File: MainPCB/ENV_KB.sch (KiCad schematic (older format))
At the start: 196 parts

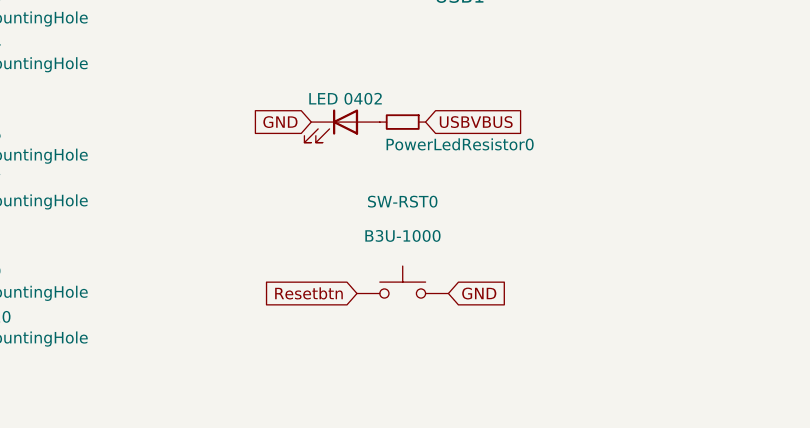
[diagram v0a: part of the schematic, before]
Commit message: Swapped Reset button for cheaper Alps SKRK
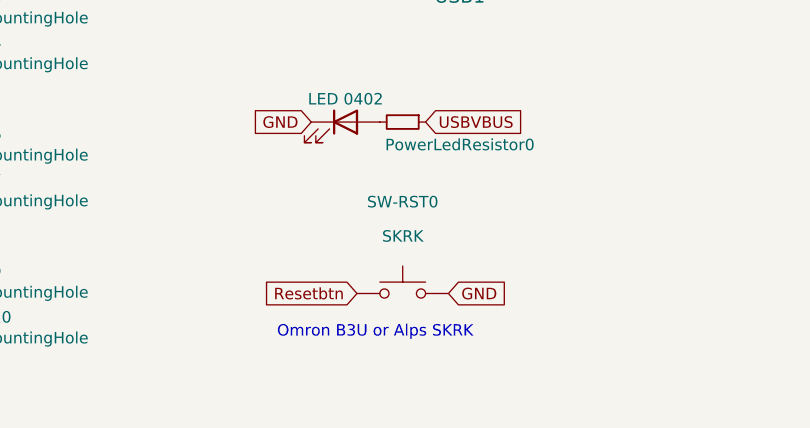
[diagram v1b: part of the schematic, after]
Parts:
- SW-RST0: value B3U-1000 -> SKRK; footprint Button_Switch_SMD:SW_SPST_B3U-1000P -> Button_Switch_SMD:SW_Push_SPST_NO_Alps_SKRK
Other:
- note added: "Omron B3U or Alps SKRK"
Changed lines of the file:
@@
 P 8550 10700
 F 0 "SW-RST0" H 8550 11100 50  0000 C CNN
-F 1 "B3U-1000" H 8550 10950 50  0000 C CNN
-F 2 "Button_Switch_SMD:SW_SPST_B3U-1000P" H 8550 10700 50  0001 L BNN
+F 1 "SKRK" H 8550 10950 50  0000 C CNN
+F 2 "Button_Switch_SMD:SW_Push_SPST_NO_Alps_SKRK" H 8550 10700 50  0001 L BNN
 F 3 "" H 8550 10700 50  0001 L BNN
 F 4 "Omron" H 8550 10700 50  0001 L BNN "MANUFACTURER"
@@
 Text GLabel 9700 8700 1    50   Input ~ 0
 USBVBUS
+Text Notes 8000 10900 0    50   ~ 0
+Omron B3U or Alps SKRK
 $EndSCHEMATC

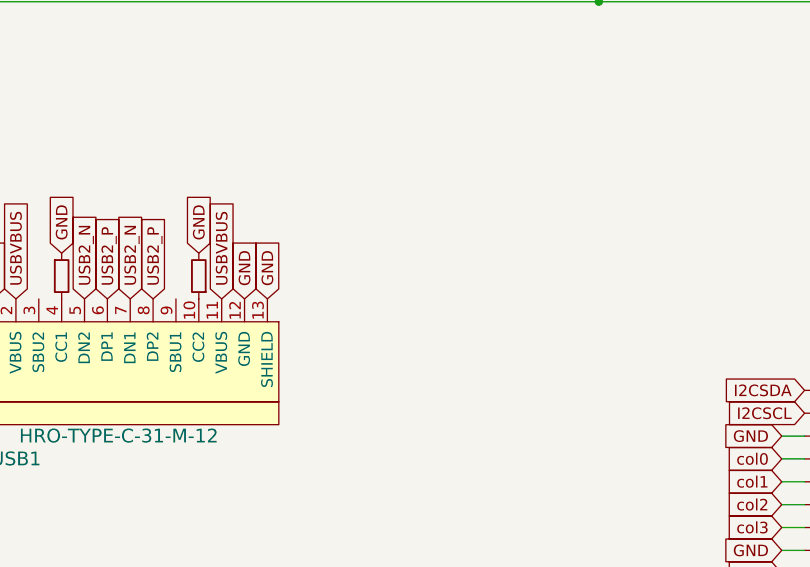
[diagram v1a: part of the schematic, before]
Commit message: added cutout for USB TP pad soldering and a JST connector in the schematic
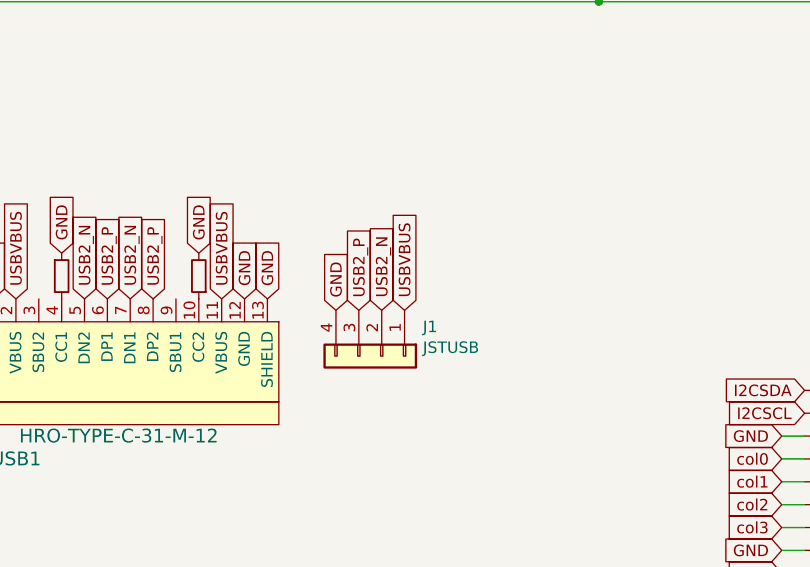
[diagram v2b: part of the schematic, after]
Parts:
- added J1: JSTUSB, Connector_JST:JST_PH_S4B-PH-SM4-TB_1x04-1MP_P2.00mm_Horizontal, symbol Connector_Generic:Conn_01x04
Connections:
- net GND: now also J1.4 (Pin_4)
- net USB2_N: now also J1.2 (Pin_2)
- net USB2_P: now also J1.3 (Pin_3)
- net USBVBUS: now also J1.1 (Pin_1)
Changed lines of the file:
@@
 Text Notes 8000 10900 0    50   ~ 0
 Omron B3U or Alps SKRK
+$Comp
+L Connector_Generic:Conn_01x04 J1
+U 1 1 61A29812
+P 10400 8950
+F 0 "J1" V 10272 9130 50  0000 L CNN
+F 1 "JSTUSB" V 10363 9130 50  0000 L CNN
+F 2 "Connector_JST:JST_PH_S4B-PH-SM4-TB_1x04-1MP_P2.00mm_Horizontal" H 10400 8950 50  0001 C CNN
+F 3 "~" H 10400 8950 50  0001 C CNN
+	1    10400 8950
+	0    1    1    0
+$EndComp
+Text GLabel 10500 8750 1    50   Input ~ 0
+USBVBUS
+Text GLabel 10200 8750 1    50   Input ~ 0
+GND
+Text GLabel 10300 8750 1    50   Input ~ 0
+USB2_P
+Text GLabel 10400 8750 1    50   Input ~ 0
+USB2_N
 $EndSCHEMATC

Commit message: cleaned up libraries and stuff, need to fix some bits probably
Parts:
- removed J1: JSTUSB, Connector_JST:JST_PH_S4B-PH-SM4-TB_1x04-1MP_P2.00mm_Horizontal, symbol Connector_Generic:Conn_01x04
- added STAB1: Stabilizer, Mounting_Keyboard_Stabilizer:Stabilizer_Cherry_MX_2u, symbol Mechanical:MountingHole
- PowerLedResistor0: value 2.2K Resistor 0402 -> 47K Resistor 0402
- SW-RST0: value SKRK -> EVQ; footprint Button_Switch_SMD:SW_Push_SPST_NO_Alps_SKRK -> Button_Switch_SMD:Panasonic_EVQPUL_EVQPUC; LCSC C231329 -> (none); MANUFACTURER Omron -> (none)
- USB1: footprint HRO-TYPE-C31-M-12:HRO-TYPE-C-31-M-12 -> josh-connectors:USB_C_TYPE-C-31-M-14; symbol Type-C:HRO-TYPE-C-31-M-12 -> josh-connector:USB_C_U262-161N-4BVC11
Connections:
- net GND: now also USB1.A1 (GND), USB1.A12 (GND), USB1.B1 (GND), USB1.B12 (GND), USB1.S1 (SHIELD); no longer USB1.1 (GND), USB1.12 (GND), USB1.13 (SHIELD)
- net USB2_N: now also USB1.A7 (D-), USB1.B7 (D-); no longer USB1.5 (DN2), USB1.7 (DN1)
- net USB2_P: now also USB1.A6 (D+), USB1.B6 (D+); no longer USB1.6 (DP1), USB1.8 (DP2)
- net USBVBUS: now also USB1.A4 (VBUS), USB1.A9 (VBUS), USB1.B4 (VBUS), USB1.B9 (VBUS); no longer USB1.11 (VBUS), USB1.2 (VBUS)
- net at RESISTOR1.2: now also USB1.A5 (CC1); no longer USB1.4 (CC1)
- net at RESISTOR0.1: now also USB1.B5 (CC2); no longer USB1.10 (CC2)
- no-connect marks 0 -> 2
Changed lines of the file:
@@
 	1350 3400 2350 3400
 Wire Wire Line
-	900  2400 2400 2400
-Wire Wire Line
 	1350 1400 3350 1400
 Wire Wire Line
@@
 Text GLabel 900  3400 0    50   Input ~ 0
 row2
-Text GLabel 900  2400 0    50   Input ~ 0
-row1
 Connection ~ 18800 950
 Wire Wire Line
@@
 Text GLabel 12950 8900 1    50   Input ~ 0
 USB2_N
-Text GLabel 9300 8700 1    50   Input ~ 0
+Text GLabel 10050 9650 0    50   Input ~ 0
 USB2_N
-Text GLabel 9400 8700 1    50   Input ~ 0
+Text GLabel 10050 9450 0    50   Input ~ 0
 USB2_P
 Text GLabel 13100 8900 1    50   Input ~ 0
@@
 Text GLabel 13650 9100 2    50   Input ~ 0
 USBVBUS
-Text GLabel 8800 8700 1    50   Input ~ 0
-USBVBUS
-Text GLabel 9000 8500 1    50   Input ~ 0
+Text GLabel 9850 10050 0    50   Input ~ 0
 GND
 Text GLabel 12150 9300 0    50   Input ~ 0
@@
 L Device:R_Small RESISTOR1
 U 1 1 606333E5
-P 9000 8600
-F 0 "RESISTOR1" V 8804 8600 39  0001 C CNN
-F 1 "5.1kohm 0402" V 9000 8700 30  0001 C CNN
-F 2 "Resistor_SMD:R_0402_1005Metric" H 9000 8600 50  0001 C CNN
-F 3 "~" H 9000 8600 50  0001 C CNN
-F 4 "C25905" V 9000 8600 50  0001 C CNN "LCSC"
-	1    9000 8600
-	1    0    0    -1
+P 9950 10050
+F 0 "RESISTOR1" V 9754 10050 39  0001 C CNN
+F 1 "5.1kohm 0402" V 9950 10150 30  0001 C CNN
+F 2 "Resistor_SMD:R_0402_1005Metric" H 9950 10050 50  0001 C CNN
+F 3 "~" H 9950 10050 50  0001 C CNN
+F 4 "C25905" V 9950 10050 50  0001 C CNN "LCSC"
+	1    9950 10050
+	0    -1   -1   0
 $EndComp
 $Comp
 L Device:R_Small RESISTOR0
 U 1 1 6066AF89
-P 9600 8600
-F 0 "RESISTOR0" V 9404 8600 39  0001 C CNN
-F 1 "5.1kohm 0402" V 9495 8600 50  0001 C CNN
-F 2 "Resistor_SMD:R_0402_1005Metric" H 9600 8600 50  0001 C CNN
-F 3 "~" H 9600 8600 50  0001 C CNN
-F 4 "C25905" V 9600 8600 50  0001 C CNN "LCSC"
-	1    9600 8600
-	-1   0    0    1
+P 9950 9950
+F 0 "RESISTOR0" V 9754 9950 39  0001 C CNN
+F 1 "5.1kohm 0402" V 9845 9950 50  0001 C CNN
+F 2 "Resistor_SMD:R_0402_1005Metric" H 9950 9950 50  0001 C CNN
+F 3 "~" H 9950 9950 50  0001 C CNN
+F 4 "C25905" V 9950 9950 50  0001 C CNN "LCSC"
+	1    9950 9950
+	0    1    1    0
 $EndComp
-Text GLabel 9600 8500 1    50   Input ~ 0
+Text GLabel 9850 9950 0    50   Input ~ 0
 GND
-Text GLabel 9800 8700 1    50   Input ~ 0
+Text GLabel 10950 8750 1    50   Input ~ 0
 GND
-Text GLabel 9900 8700 1    50   Input ~ 0
+Text GLabel 10650 8750 1    50   Input ~ 0
 GND
-Text GLabel 9100 8700 1    50   Input ~ 0
-USB2_N
-Text GLabel 9200 8700 1    50   Input ~ 0
+Text GLabel 10050 9550 0    50   Input ~ 0
 USB2_P
 $Comp
@@
 P 8550 9950
 F 0 "PowerLedResistor0" V 8650 10200 50  0000 C CNN
-F 1 "2.2K Resistor 0402" V 8700 10000 50  0001 C CNN
+F 1 "47K Resistor 0402" V 8700 10000 50  0001 C CNN
 F 2 "Resistor_SMD:R_0402_1005Metric" H 8550 9950 50  0001 C CNN
 F 3 "~" H 8550 9950 50  0001 C CNN
@@
 	0    1    1    0
 $EndComp
-Text GLabel 8700 8700 1    50   Input ~ 0
-GND
 $Comp
 L Connector_Generic:Conn_01x04 I2CHeader0
@@
 P 8550 10700
 F 0 "SW-RST0" H 8550 11100 50  0000 C CNN
-F 1 "SKRK" H 8550 10950 50  0000 C CNN
-F 2 "Button_Switch_SMD:SW_Push_SPST_NO_Alps_SKRK" H 8550 10700 50  0001 L BNN
+F 1 "EVQ" H 8550 10950 50  0000 C CNN
+F 2 "Button_Switch_SMD:Panasonic_EVQPUL_EVQPUC" H 8550 10700 50  0001 L BNN
 F 3 "" H 8550 10700 50  0001 L BNN
-F 4 "Omron" H 8550 10700 50  0001 L BNN "MANUFACTURER"
-F 5 "C231329" H 8550 10700 50  0001 C CNN "LCSC"
 	1    8550 10700
 	1    0    0    -1
@@
 $EndComp
 $Comp
-L Type-C:HRO-TYPE-C-31-M-12 USB1
+L josh-connector:USB_C_U262-161N-4BVC11 USB1
 U 1 1 60AC4D40
-P 9250 8800
-F 0 "USB1" V 8650 9250 60  0000 C CNN
-F 1 "HRO-TYPE-C-31-M-12" V 8750 8800 60  0000 C CNN
-F 2 "HRO-TYPE-C31-M-12:HRO-TYPE-C-31-M-12" H 9250 8800 60  0001 C CNN
-F 3 "" H 9250 8800 60  0001 C CNN
-F 4 "C165948" H 9250 8800 50  0001 C CNN "LCSC"
-	1    9250 8800
-	0    -1   -1   0
+P 10650 9650
+F 0 "USB1" V 10050 10100 60  0000 C CNN
+F 1 "HRO-TYPE-C-31-M-12" V 10150 9650 60  0000 C CNN
+F 2 "josh-connectors:USB_C_TYPE-C-31-M-14" H 10650 9650 60  0001 C CNN
+F 3 "" H 10650 9650 60  0001 C CNN
+F 4 "C165948" H 10650 9650 50  0001 C CNN "LCSC"
+	1    10650 9650
+	-1   0    0    1
 $EndComp
-Text GLabel 9700 8700 1    50   Input ~ 0
+Text GLabel 10050 10250 0    50   Input ~ 0
 USBVBUS
 Text Notes 8000 10900 0    50   ~ 0
 Omron B3U or Alps SKRK
+Text GLabel 10050 9750 0    50   Input ~ 0
+USB2_N
+NoConn ~ 10050 9150
+NoConn ~ 10050 9050
 $Comp
-L Connector_Generic:Conn_01x04 J1
-U 1 1 61A29812
-P 10400 8950
-F 0 "J1" V 10272 9130 50  0000 L CNN
-F 1 "JSTUSB" V 10363 9130 50  0000 L CNN
-F 2 "Connector_JST:JST_PH_S4B-PH-SM4-TB_1x04-1MP_P2.00mm_Horizontal" H 10400 8950 50  0001 C CNN
-F 3 "~" H 10400 8950 50  0001 C CNN
-	1    10400 8950
-	0    1    1    0
+L Mechanical:MountingHole STAB1
+U 1 1 61D508CB
+P 7650 8700
+F 0 "STAB1" H 7750 8746 50  0000 L CNN
+F 1 "Stabilizer" H 7750 8655 50  0000 L CNN
+F 2 "Mounting_Keyboard_Stabilizer:Stabilizer_Cherry_MX_2u" H 7650 8700 50  0001 C CNN
+F 3 "~" H 7650 8700 50  0001 C CNN
+	1    7650 8700
+	1    0    0    -1
 $EndComp
-Text GLabel 10500 8750 1    50   Input ~ 0
-USBVBUS
-Text GLabel 10200 8750 1    50   Input ~ 0
-GND
-Text GLabel 10300 8750 1    50   Input ~ 0
-USB2_P
-Text GLabel 10400 8750 1    50   Input ~ 0
-USB2_N
 $EndSCHEMATC
